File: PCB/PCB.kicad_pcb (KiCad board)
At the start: 2 copper layers, 120 x 60 mm, 63 parts, among them J1 USB_C_Receptacle_USB2.0_16P, J2 Conn_01x15, J3 Conn_01x15, Q2 IRLML2060, SW1 TSA016A2526B, SW2 TSA016A2526B, SW3 TSA016A2526B, U1 RP2040, U2 USBLC6-2SC6, U3 NCP1117ST33T3G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

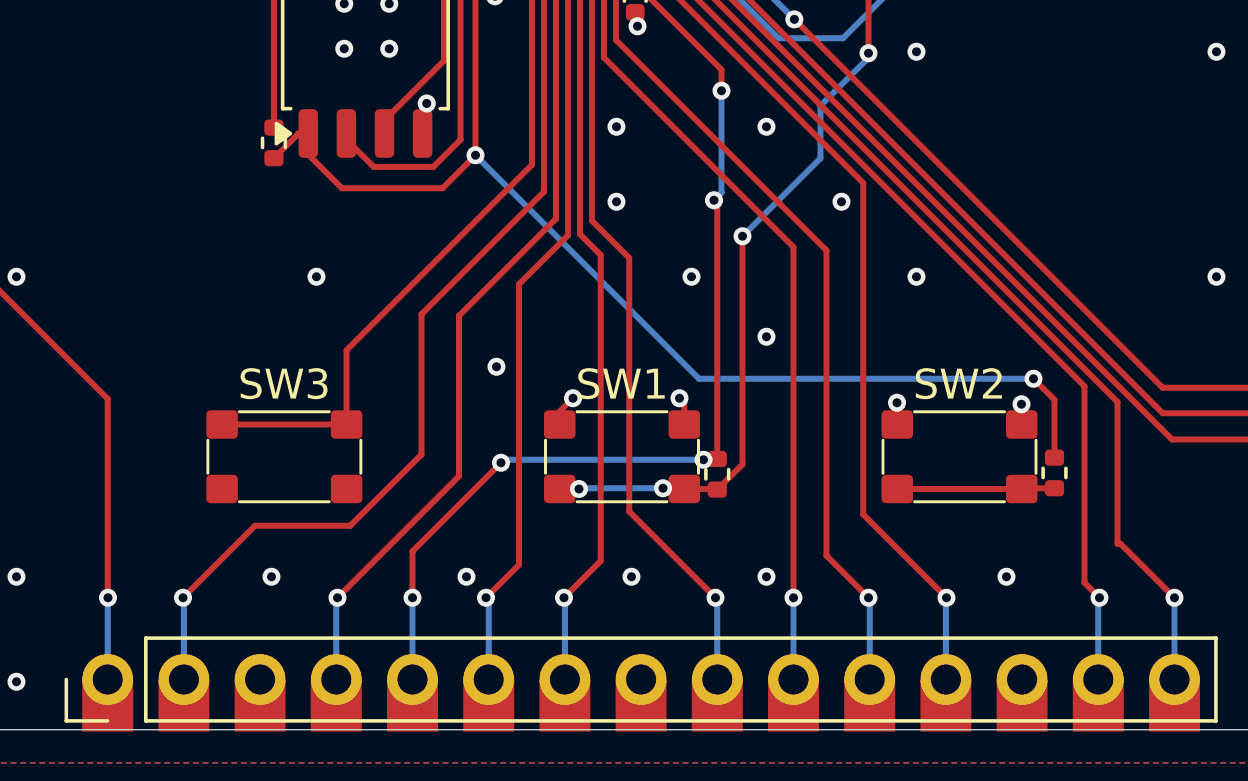
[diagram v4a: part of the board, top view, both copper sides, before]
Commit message: moved the buttons, new prod files
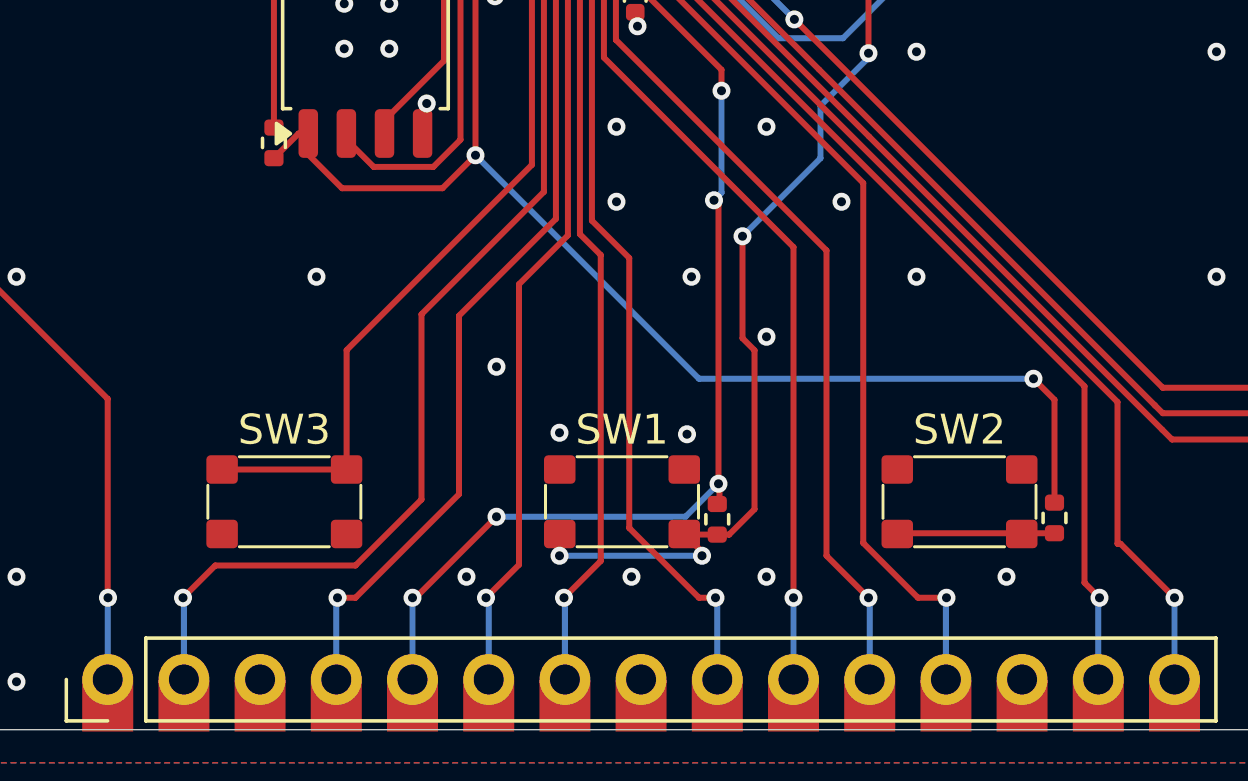
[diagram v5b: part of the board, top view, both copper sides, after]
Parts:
- moved R5 1.50 mm to (143.4, 78.1)
- moved R9 1.50 mm to (154.6, 78.0)
- moved SW1 1.50 mm to (140.2, 77.5)
- moved SW2 1.50 mm to (151.4, 77.5)
- moved SW3 1.50 mm to (128.9, 77.5)
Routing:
- net /RESET: track 35.9 -> 40.2 mm
- net GND: track 46.8 -> 43.4 mm, vias 124 -> 121
- net /QSPI_SS: track 42.0 -> 43.5 mm
- net Net-(U1-GPIO0): track 23.3 -> 24.8 mm
- net /GPIO1: track 31.8 -> 32.7 mm
- net /GPIO8: track 29.2 -> 29.7 mm

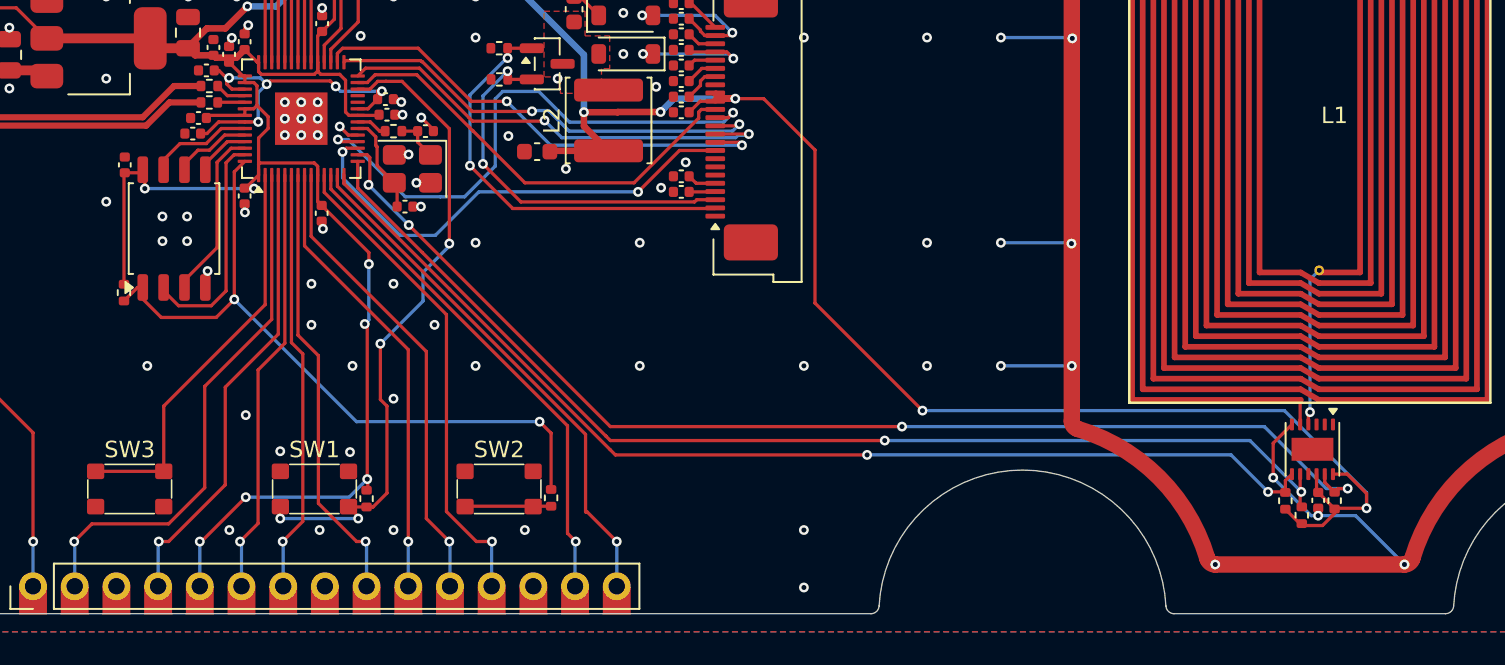
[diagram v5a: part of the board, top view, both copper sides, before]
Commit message: cleaned up the silkscreen and added load cap to antenna
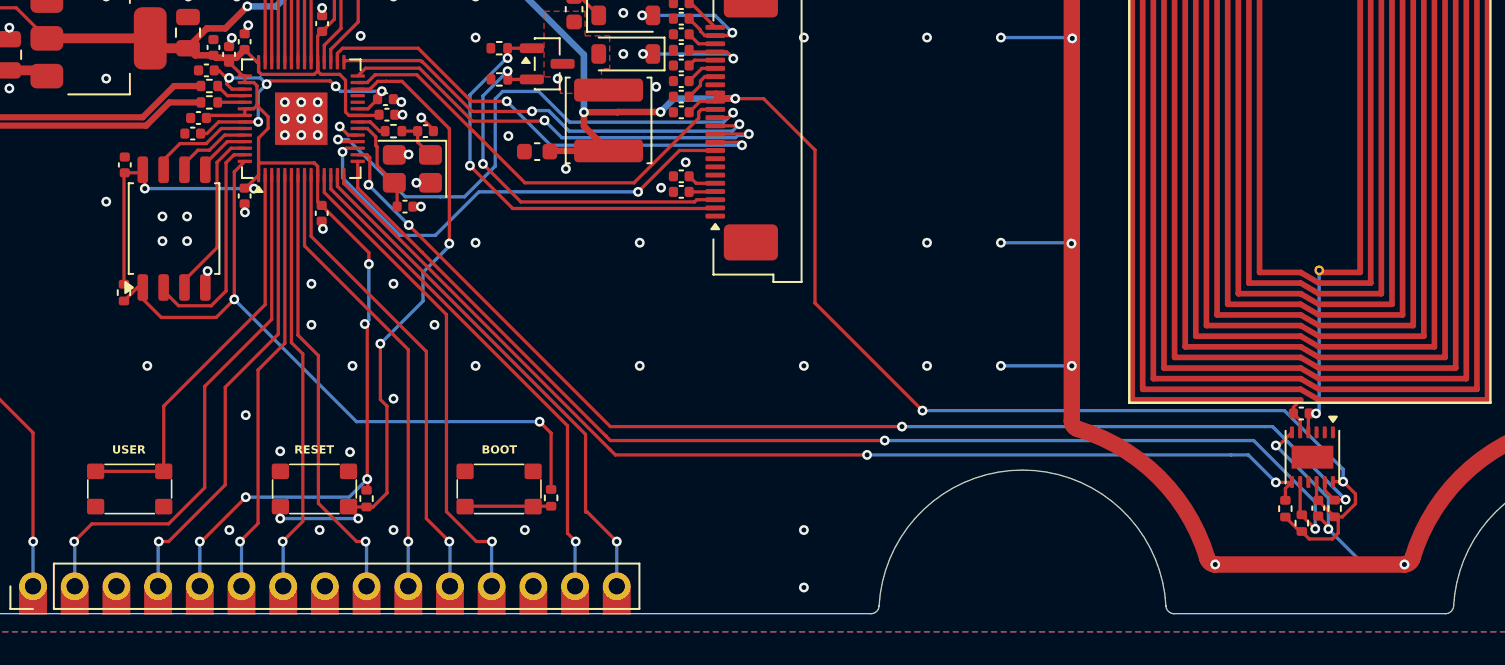
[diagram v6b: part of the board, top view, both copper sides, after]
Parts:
- added C30: 33pF, Capacitor_SMD:C_0402_1005Metric, F.Cu at (200.3, 72.9)
- moved C29 0.48 mm to (201.3, 78.7)
- moved R10 0.48 mm to (199.3, 78.7)
- moved R13 0.48 mm to (200.3, 79.6)
- moved R14 0.48 mm to (202.3, 78.7)
- moved U6 0.48 mm to (201.0, 75.6)
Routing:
- net /NFC_SCL: track 68.8 -> 72.7 mm
- net +3V3: track 262.8 -> 260.1 mm
- net Net-(U6-AC1): track 1.51 -> 2.33 mm
- net Net-(U6-AC0): track 9.67 -> 10.4 mm
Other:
- board text added: "BOOT"
- board text added: "RESET"
- board text added: "USER"

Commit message: new inductor a bit pissed about it
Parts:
- L2: footprint Inductor_SMD:L_Sunlord_SWPA5020S -> Inductor_SMD:L_Changjiang_FNR6028S
- moved L2 0.48 mm to (158.3, 55.5)
- moved C28 0.35 mm to (153.5, 57.2)
- moved Q2 0.28 mm to (154.1, 51.5)
- moved R11 0.28 mm to (151.2, 50.6)
- moved R12 0.28 mm to (151.2, 52.5)
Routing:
- net +3V3: track 260.1 -> 261.7 mm
- net /EPD_MOSI: track 26.8 -> 27.6 mm
- net GND: track 43.3 -> 43.9 mm, vias 121 -> 118

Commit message: adding in the art :D
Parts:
- added G***: LOGO, LOGO, B.Cu at (163.9, 56.7)
- added G***: LOGO, LOGO, B.Cu at (163.9, 56.8)
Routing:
- net /RESET: track 40.2 -> 46.2 mm
- net +3V3: track 261.7 -> 264.7 mm
- net +1V1: track 21.3 -> 24.2 mm, vias 5 -> 4
- net +5V: track 119.1 -> 120.9 mm
- net GND: track 43.9 -> 43.8 mm, vias 118 -> 115
